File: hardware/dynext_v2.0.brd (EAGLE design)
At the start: 35.3 x 17.8 mm, 41 parts, among them P1 PIN_SMD_2X2.5, P2 PIN_SMD_2X2.5, P3 PIN_SMD_0.8X2, P4 PIN_SMD_0.8X2, U2 LD6805K/33P, U3 IC_ATMEGA328P-MMH, U4 TXB0101DCK, U6 LPC11A02UK,118, Y1 CSTCE16M0V53

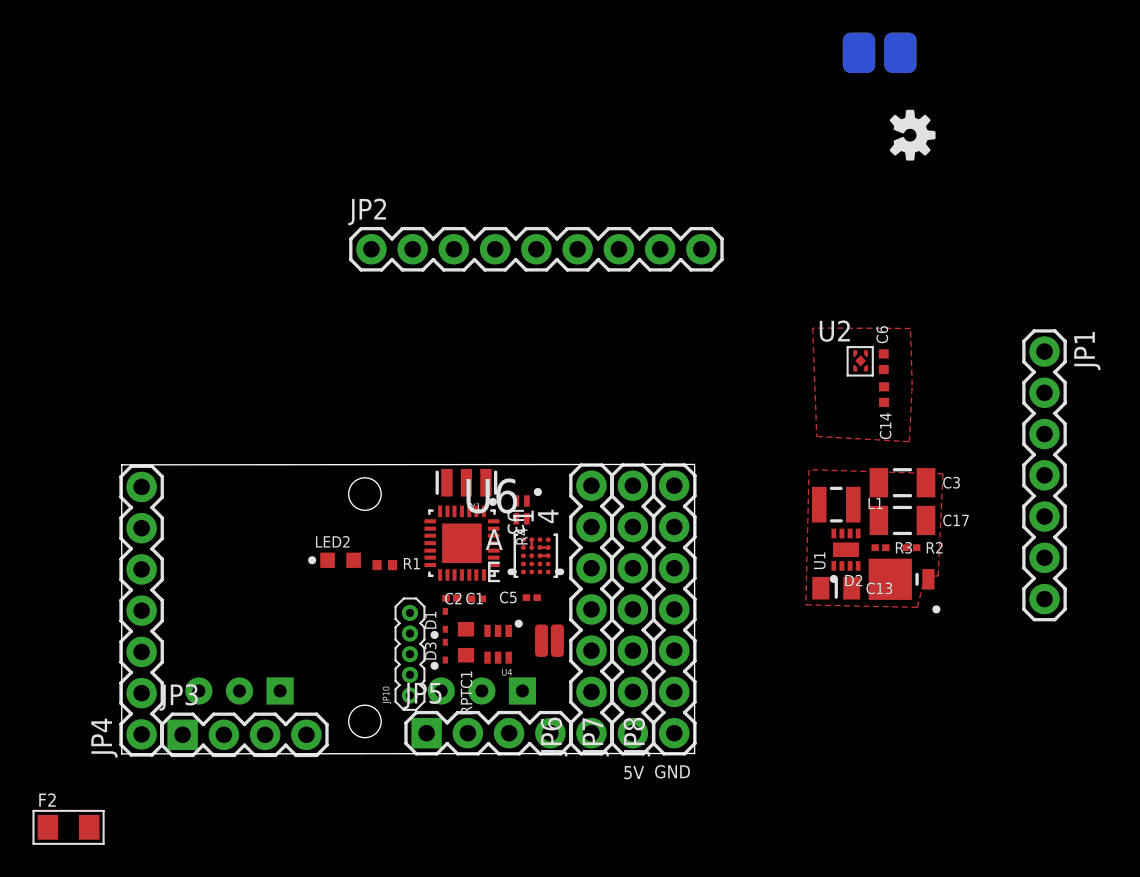
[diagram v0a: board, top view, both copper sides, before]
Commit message: Shifting things around, preparing for the real pinout & layout.
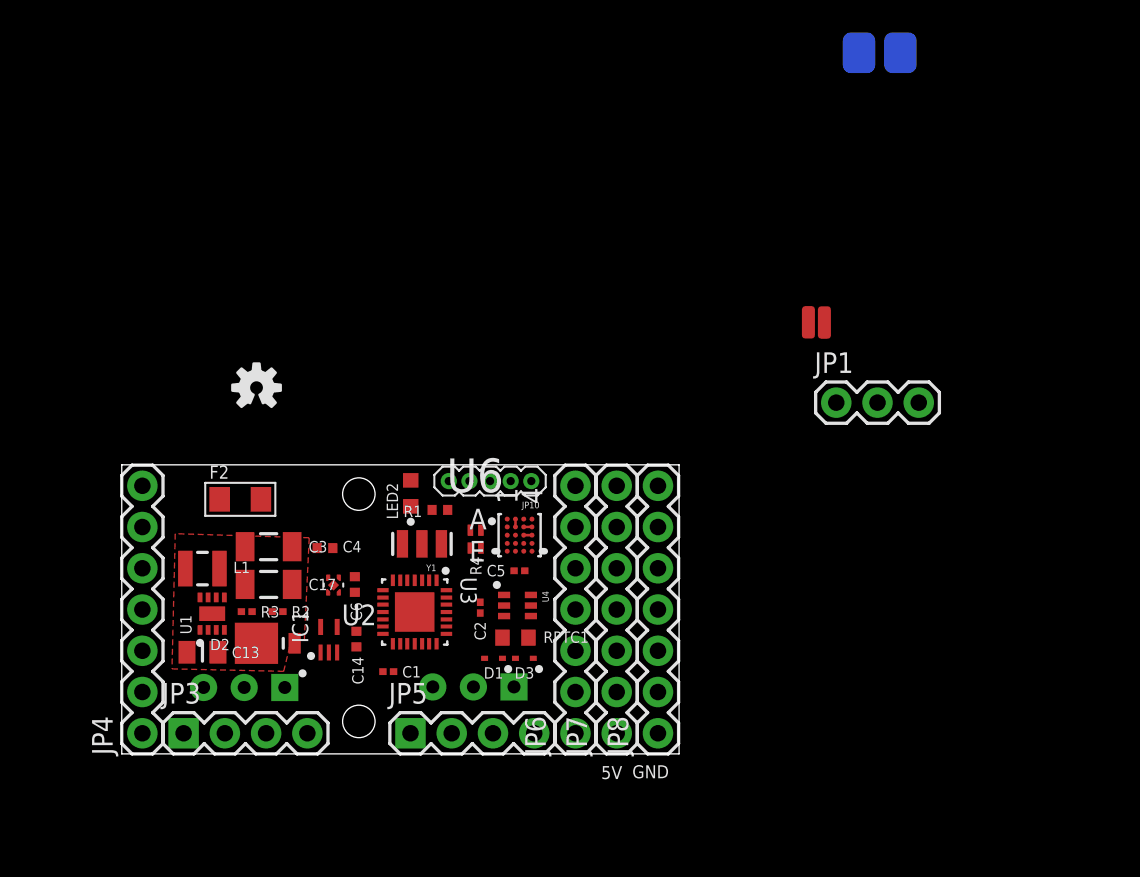
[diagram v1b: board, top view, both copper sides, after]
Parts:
- removed JP2: M09, SparkFun-Connectors:1X09
- added C4: 1uF, Xevelabs:0402_N
- added IC1: TCR2EE50,LM, Xevelabs:SOT50P160X60-5N
- JP1: device SparkFun-Connectors:1X07 -> SparkFun-Connectors:1X03
- moved U$1 43.1 mm to (8.30, 22.6), turned to 0 degrees
- moved C13 39.2 mm to (4.97, 6.26)
- moved C17 39.2 mm to (9.04, 10.4)
- moved C3 39.2 mm to (9.04, 12.8)
- moved D2 39.2 mm to (8.99, 6.81)
- moved L1 39.2 mm to (4.97, 11.4)
- moved R2 39.2 mm to (9.60, 8.76)
- moved R3 39.2 mm to (7.70, 8.76)
- moved U1 39.2 mm to (5.57, 8.63)
- moved C14 35.8 mm to (14.4, 7.07)
- moved C6 35.3 mm to (14.4, 10.4), turned to 270 degrees
- moved U2 35.3 mm to (13.0, 10.4), turned to 180 degrees
- moved P4 26.2 mm to (43.3, 26.6)
- moved P3 25.0 mm to (42.3, 26.6)
- moved F2 22.8 mm to (7.30, 15.7)
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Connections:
- net D13 renamed D13/LED
- removed net PA2: JP1.3
- removed net PA3: JP1.4
- removed net PA7: JP1.5
- removed net PC0: JP1.6
- removed net PC1: JP1.7
- removed net PC4: JP2.7
- removed net PC5: JP2.6
- removed net PC6: JP2.5
- removed net PC7: JP2.4
- net +3V3: now also C6.1, U2.1; no longer C14.1, JP1.2
- net +5V: now also C14.1, IC1.4; no longer C6.1, JP2.2, U2.1
- net 5.25V: now also C4.1, IC1.1, IC1.3
- net AREF: no longer JP2.3
- net GND: now also C4.2, IC1.2, IC1.5; no longer JP1.1, JP2.1
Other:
- board size 35.3 x 17.8 mm -> 34.3 x 17.8 mm

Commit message: Schematics stabilized, routing in half-way done.
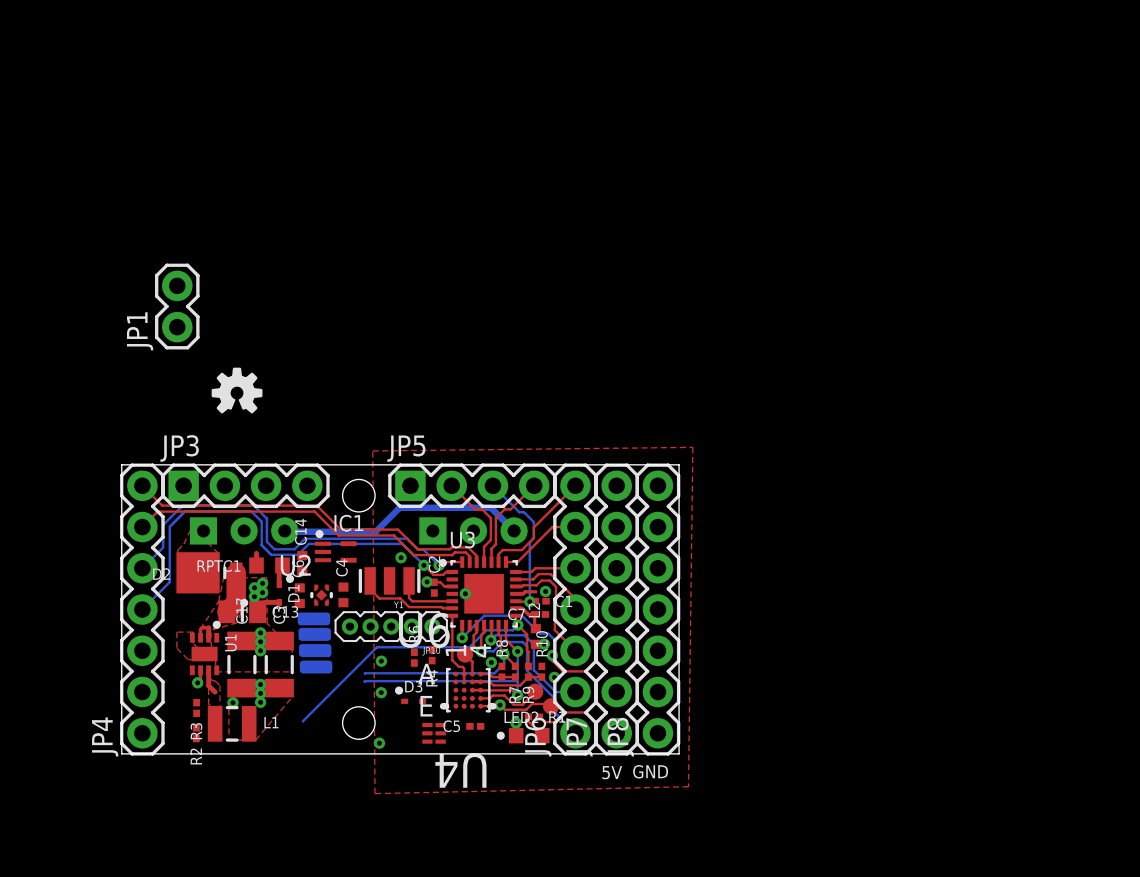
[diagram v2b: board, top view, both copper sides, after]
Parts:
- removed F2: TODO, OPL:F1206
- added C7: 0.1uF, Xevelabs:0201_N
- added L2: ferrite, Xevelabs:0402_N
- added P5: PIN_SMD_0.8X2, Xevelabs:PIN_SMD_0.8X2
- added P6, P7: PIN_SMD_1X1, Xevelabs:PIN_SMD_1X1
- added R10, R7, R8, R9: 10K, Xevelabs:0201_N
- added R6: 47k, Xevelabs:0201_N
- JP1: value (none) -> M02PTH; device SparkFun-Connectors:1X03 -> SparkFun-Connectors:1X02
- P1: value PIN_SMD_2X2.5 -> PIN_SMD_0.8X2; device Xevelabs:PIN_SMD_2X2.5 -> Xevelabs:PIN_SMD_0.8X2
- P2: value PIN_SMD_2X2.5 -> PIN_SMD_1X1; device Xevelabs:PIN_SMD_2X2.5 -> Xevelabs:PIN_SMD_1X1
- R1: device Xevelabs:0402_N -> Xevelabs:0201_N
- R4: device Xevelabs:ARRAY_0402_65P_2_N -> Xevelabs:0201_N
- U1: value (none) -> TPS62160DSG
- U4: value TXB0101DCK -> TXB0101DRL; device MWquad_stuff:SC70-6 -> Xevelabs:SON50P105X150X60-6N
- moved P1 49.1 mm to (11.9, 7.36), turned to 0 degrees
- moved P2 45.6 mm to (26.4, 2.93), flipped to the top, turned to 0 degrees
- moved JP1 40.8 mm to (3.42, 26.3), turned to 90 degrees
- moved P4 37.8 mm to (12.0, 5.35), flipped to the bottom, turned to 0 degrees
- moved P3 35.5 mm to (11.8, 8.31), flipped to the bottom, turned to 0 degrees
- moved DXL1 21.4 mm to (5.04, 13.7), turned to 270 degrees
- moved LED2 16.6 mm to (25.1, 1.12), turned to 0 degrees
- moved RPTC1 15.8 mm to (9.10, 11.6), turned to 180 degrees
- moved JP3 15.2 mm to (3.81, 16.5)
- moved JP5 15.2 mm to (17.8, 16.5)
- moved R1 14.0 mm to (25.4, 2.28), turned to 0 degrees
- moved D1 13.8 mm to (9.70, 9.88), turned to 270 degrees
- moved DXL2 13.3 mm to (19.2, 13.7), turned to 270 degrees
- moved JP10 10.8 mm to (19.1, 7.84)
- moved C1 10.3 mm to (25.8, 9.40)
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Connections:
- removed net D13/LED: R1.2
- removed net DATA_RX: P3.PIN, U6.E1
- removed net DATA_TX: P4.PIN, U6.D1
- removed net MISO: U6.C3, U6.C4
- removed net N$13: U3.16
- removed net N$7: D1.C, D3.A, RPTC1.1, U4.4
- removed net PD0: P1.PIN
- removed net PD1: P2.PIN
- removed net SSEL/ISP: U6.A2, U6.B2
- removed net UART0: U4.3
- new net A0: JP6.3, U3.19
- new net A1: JP6.4, U3.20
- new net A2: JP6.5, U3.21
- new net A3: JP6.6, U3.22
- new net A4: JP6.7, U3.23
- new net A5: JP5.4, U3.24
- new net ARDU_RST: JP5.2, U3.25
- new net AVCC: C7.2, L2.2, U3.16
- new net D0: JP4.7, U3.26
- new net D1: JP4.6, U3.27
- new net D10: JP6.2, U3.12
- new net D11: JP4.3, R7.1, U3.13
- new net D13: JP4.1, R9.1, U3.15
- new net D2: JP4.5, U3.28
- new net D3: JP4.4, U3.1
- new net D6(LED): R1.2, U3.8
- new net D9: JP6.1, U3.11
- new net LPC_INT: P6.P$1, U3.10, U6.A3
- new net LPC_RX: D1.C, D3.A, P5.PIN, RPTC1.1, U4.4, U6.E1
- new net LPC_TX: P4.PIN, U4.3, U6.D1
- new net MISO/D12: JP4.2, U3.14, U6.C3, U6.C4
- new net N$1: P7.P$1, U6.D4
- new net SSEL/ISP/D5: P3.PIN, U3.7, U6.A2, U6.B2
- new net TX_EN: P2.P$1, U4.5, U6.E4
- net +3V3: now also JP3.4, R4.1, R6.2; no longer R4.3, R4.4, U4.5
- net +5V: now also JP3.2, JP7.3, JP7.4, JP7.5, JP7.6, JP7.7, L2.1
- net 5.25V: now also JP1.1, JP7.1, JP7.2
- net AREF: now also JP5.3
- net GND: now also C7.1, JP1.2, JP3.1, JP3.3, JP5.1, JP8.1, JP8.2, JP8.3, JP8.4, JP8.5, JP8.6, JP8.7, P1.PIN, R10.2, R8.2
- net LPC_RST: now also JP10.4
- net MOSI: now also R7.2, R8.1
- net SCK: now also R10.1, R9.2
- net SWCLK: now also JP10.2, R6.1; no longer R4.1
- net SWDIO: now also JP10.3
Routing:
- net D3: track 0.00 -> 26.7 mm, vias 0 -> 1
- net D2: track 0.00 -> 25.1 mm, vias 0 -> 1
- net D0: track 0.00 -> 22.8 mm
- net D1: track 0.00 -> 22.2 mm
- net D13: track 0.00 -> 19.1 mm, vias 0 -> 1
- net D6(LED): track 0.00 -> 17.6 mm, vias 0 -> 2
- net MISO/D12: track 0.00 -> 16.9 mm, vias 0 -> 2
- net DATA: track 0.00 -> 16.1 mm
- net D11: track 0.00 -> 12.3 mm, vias 0 -> 1
- net D9: track 0.00 -> 11.4 mm, vias 0 -> 1
- net AREF: track 0.00 -> 9.67 mm, vias 0 -> 1
- net D10: track 0.00 -> 8.61 mm, vias 0 -> 1
- net A4: track 0.00 -> 7.35 mm
- net A0: track 0.00 -> 7.27 mm
- net ARDU_RST: track 0.00 -> 6.12 mm
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- added copper zone on layer 1, net +12V
- added copper zone on layer 1, net 5.25V
- added copper zone on layer 3, net 5.25V
- added copper zone on layer 1, net N$2
- removed copper zone on layer 3, net +3V3
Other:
- board text added: "v2.0"
- board text removed: "5"
- board text removed: "A2"
- board text removed: "A3"
- board text removed: "A7"
- board text removed: "C0"
- board text removed: "C1"
- board text removed: "C4"
- board text removed: "C5"
- board text removed: "C6"
- board text removed: "C7"
- board text removed: "D0"
- board text removed: "D1"
- board text removed: "J1"
- board text removed: "J2"
- board text removed: "PDI"
- board text removed: "REF"
- board text removed: "v1.1"

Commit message: Routing is getting close to something viable. I probably will rip up some of the most complex parts to simplifiy them ><
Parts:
- U4: value TXB0101DRL -> TXB0101DCK; device Xevelabs:SON50P105X150X60-6N -> Xevelabs:SC70-6
- moved JP1 41.3 mm to (36.3, 1.32)
- moved P3 11.9 mm to (20.8, 0.41), turned to 270 degrees
- moved P1 10.3 mm to (19.5, 0.41), turned to 270 degrees
- moved P4 7.98 mm to (18.2, 0.41), turned to 270 degrees
- moved U2 7.95 mm to (9.99, 2.17), turned to 90 degrees
- moved P5 7.80 mm to (17.0, 0.41), turned to 270 degrees
- moved C6 7.57 mm to (11.4, 2.18)
- moved R6 4.57 mm to (14.9, 9.28), turned to 180 degrees
- moved R2 4.23 mm to (3.53, 5.37)
- moved R4 4.22 mm to (14.9, 6.55), turned to 0 degrees
- moved R3 4.21 mm to (3.53, 6.89), turned to 90 degrees
- moved IC1 3.62 mm to (11.3, 9.33), turned to 90 degrees
- moved C4 3.10 mm to (11.8, 7.30), turned to 180 degrees
- moved U4 2.94 mm to (18.0, 3.93)
- moved D3 1.30 mm to (18.0, 1.94), turned to 180 degrees
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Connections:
- net +3V3: now also JP3.2; no longer JP3.4
- net +5V: now also JP3.4; no longer JP3.2
- net GND: no longer IC1.5
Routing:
- net D11: track 12.3 -> 39.6 mm
- net MISO/D12: track 16.9 -> 42.4 mm
- net LPC_RX: track 1.26 -> 22.7 mm, vias 0 -> 3
- net +3V3: track 0.00 -> 19.1 mm, vias 1 -> 2
- net D13: track 19.1 -> 35.9 mm, vias 1 -> 2
- net +5V: track 2.63 -> 17.4 mm, vias 3 -> 4
- net SSEL/ISP/D5: track 4.50 -> 17.6 mm, vias 0 -> 1
- net GND: track 2.16 -> 13.1 mm, vias 14 -> 16
- net 5.25V: track 0.85 -> 10.8 mm
- net LPC_TX: track 0.00 -> 9.64 mm, vias 0 -> 1
- net LPC_RST: track 0.00 -> 7.64 mm, vias 0 -> 1
- net SWDIO: track 0.00 -> 7.58 mm
- net SWCLK: track 0.00 -> 7.44 mm
- net TX_EN: track 4.70 -> 10.9 mm, vias 1 -> 2
- net +12V: track 4.33 -> 7.11 mm
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- added copper zone on layer 3, net +3V3

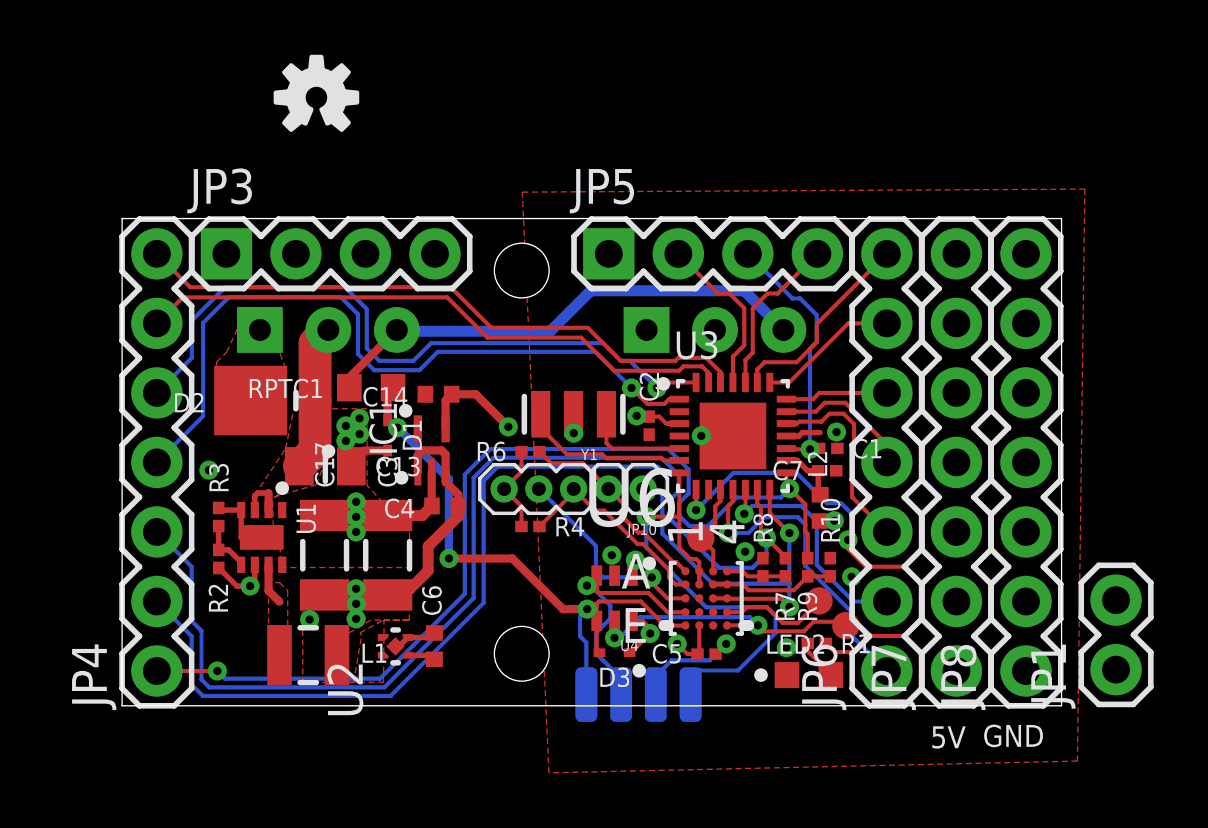
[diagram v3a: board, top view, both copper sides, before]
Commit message: Routing roughly done and seems OK. More verif and silkscreen still needed.
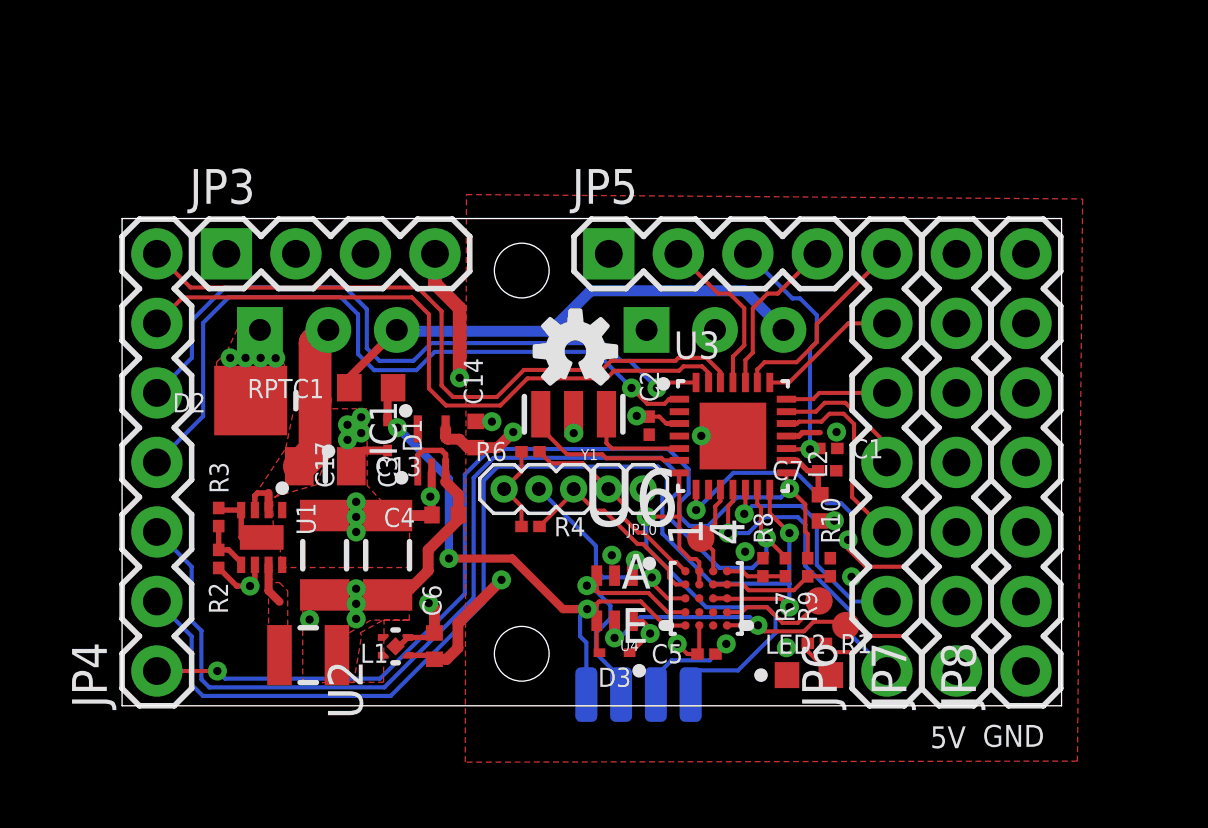
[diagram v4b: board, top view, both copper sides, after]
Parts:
- removed JP1: M02PTH, SparkFun-Connectors:1X02
- moved U$1 13.2 mm to (16.6, 12.9)
- moved C14 2.00 mm to (12.9, 9.91), turned to 90 degrees
- moved C4 0.33 mm to (11.8, 6.97)
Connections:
- net 5.25V: no longer JP1.1
- net GND: no longer JP1.2
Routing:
- net N$16: track 0.00 -> 19.8 mm
- net N$4: track 0.00 -> 18.3 mm
- net N$8: track 0.00 -> 5.37 mm
- net N$7: track 0.00 -> 4.68 mm
- net +3V3: track 19.1 -> 23.3 mm, vias 2 -> 3
- net D0: track 22.8 -> 25.5 mm
- net D1: track 22.2 -> 24.8 mm
- net N$14: track 0.00 -> 2.36 mm
- net GND: track 13.1 -> 15.1 mm, vias 16 -> 22
- net N$11: track 0.00 -> 1.89 mm
- net N$5: track 0.00 -> 1.68 mm
- net +5V: track 17.4 -> 18.8 mm, vias 4 -> 5
- net N$15: track 0.00 -> 0.68 mm

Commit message: Added all the silkscreen. Potentially ready.
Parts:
- JP3, JP5: device SparkFun-Connectors:1X04 -> SparkFun-Connectors:1X04_NO_SILK
- JP4, JP6, JP7: device SparkFun-Connectors:1X07 -> Xevelabs:1X07_NO_SILK
- JP8: device SparkFun-Connectors:1X07 -> Xevelabs:1X07_SQUARE_ALL
- U6: value LPC11A02UK,118 -> IC_LPC11A0UK,118
- moved U$1 2.00 mm to (14.6, 13.3), turned to 180 degrees
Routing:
- net N$14: track 2.36 -> 1.81 mm
- net GND: vias 22 -> 15
- net 5.25V: vias 5 -> 4
- added copper zone on layer 16, net GND
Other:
- outline, holes or cut-outs redrawn
- board text added: "0"
- board text added: "1"
- board text added: "10"
- board text added: "11"
- board text added: "12"
- board text added: "13"
- board text added: "2"
- board text added: "3"
- board text added: "5/ISP"
- board text added: "5V 150mA"
- board text added: "5V 800mA"
- board text added: "9"
- board text added: "A0"
- board text added: "A1"
- board text added: "A2"
- board text added: "A3"
- board text added: "A4"
- board text added: "A5"
- board text added: "AREF"
- board text added: "RST"
- board text added: "RX"
- board text added: "TX"
- board text added: "XEVELABS.COM"
- board text removed: "Universal Dynamixel Device"
- board text removed: "xevelabs.com"
